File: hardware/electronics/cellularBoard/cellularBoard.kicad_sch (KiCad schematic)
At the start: 15 parts, among them J1 Standoff, J2 M.2_E_Key_PCB_Edge, U1 LM51571-Q1

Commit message: started on schematics
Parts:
- added C1: 2.2uF, symbol lib_sch:C
- added C11: 10nF, symbol lib_sch:C_horizontal
- added C12: 300pF, symbol lib_sch:C
- added C13: 1uF, symbol lib_sch:C_horizontal
- added C14: 10nF, symbol lib_sch:C
- added C15: 22uF, symbol lib_sch:C
- added C16, C2: 100nF, symbol lib_sch:C
- added D1: VAL, symbol DS-Diodes:D_Schottky_horizontal
- added L2: 680nH, symbol DS-Passives:L_horizontal
- added R1: 301R, symbol lib_sch:R
- added R2: 9K31, symbol lib_sch:R_horizontal
- added R3: 6K98, symbol lib_sch:R
- added R6: 2K49, symbol lib_sch:R
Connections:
- net VSS: now also U1.1 (PGND), U1.11 (MODE), U1.16 (PGND), U1.17 (AGND), U1.7 (AGND), C1.2, C11.1, C12.2, C13.1, C15.2, C16.2, C2.2, R1.2, R2.1
- net at U1.10 (SS): now also C11.2
- net at U1.12 (SW), U1.13 (SW), U1.14 (SW): now also D1.1, L2.2
- net at U1.2 (VCC): now also C13.2
- net at U1.3 (BIAS): now also U1.6 (UVLO), C1.1, C2.1, L2.1
- net at U1.5 (RT): now also R2.2
- net at U1.8 (COMP): now also C12.1, C14.1
- net at U1.9 (FB): now also R3.2, R6.1
- new net: C14.2, R1.1
- new net: C15.1, C16.1, D1.2, R3.1
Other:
- moved on the sheet: TP1, TP2, TP3, TP4, TP5, TP6, TP7, TP8, U1

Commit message: finished schematic
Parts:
- removed C11: 10nF, symbol lib_sch:C_horizontal
- removed C12: 300pF, symbol lib_sch:C
- removed C14: 10nF, symbol lib_sch:C
- removed C16: 100nF, symbol lib_sch:C
- removed R2: 9K31, symbol lib_sch:R_horizontal
- added C10, C19: 150pF, lib_fp:MLCC0603, symbol lib_sch:C
- added C11, C6, C9: 10nF, lib_fp:MLCC0603, symbol lib_sch:C
- added C5: 100nF, lib_fp:MLCC0603, symbol lib_sch:C
- added C7: 68pF, lib_fp:MLCC0603, symbol lib_sch:C
- added C8: 15pF, lib_fp:MLCC0603, symbol lib_sch:C
- added R3: 9K31, lib_fp:CRCW0402, symbol lib_sch:R
- added R5, R6: 10K, symbol lib_sch:R
- C1: footprint (none) -> lib_fp:MLCC0603; DKPN (none) -> 478-KAM15AR70J225KTCT-ND; MPN (none) -> KAM15AR70J225KT; Manufacturer (none) -> KYOCERA AVX; Package PKG -> 0603; Tolerance TOL -> 10%; Voltage Rating VOLTAGE -> 6V3
- C2: footprint (none) -> lib_fp:MLCC0603; DKPN (none) -> 478-KAM15AR71A104KTCT-ND; MPN (none) -> KAM15AR71A104KT; Manufacturer (none) -> KYOCERA AVX; Package PKG -> 0603; Tolerance TOL -> 10%; Voltage Rating VOLTAGE -> 10V
- C3: renamed from C13; footprint (none) -> lib_fp:MLCC0603; DKPN (none) -> 478-KAM15AR71A105KTCT-ND; MPN (none) -> KAM15AR71A105KT; Manufacturer (none) -> KYOCERA AVX; Package PKG -> 0603; Tolerace TOL -> 10%; Voltage Rating VOLT -> 10V
- C4: renamed from C15; DKPN (none) -> 478-KAM21AT70J226KUCT-ND; MPN (none) -> KAM21AT70J226KU; Manufacturer (none) -> KYOCERA AVX; Package PKG -> 0805; Tolerance TOL -> 10%; Voltage Rating VOLTAGE -> 6V3
- R1: renamed from R3; footprint (none) -> lib_fp:CRCW0402; DKPN (none) -> 541-6.98KLCT-ND; MPN (none) -> CRCW04026K98FKED; Manufacturer (none) -> Vishay Dale; Package PKG -> 0402; Power Rating PWR -> 62.5mW; Tolerance TOL -> 1%
- R2: renamed from R6; footprint (none) -> lib_fp:CRCW0402; DKPN (none) -> 541-2.49KLCT-ND; MPN (none) -> CRCW04022K49FKED; Manufacturer (none) -> Vishay Dale; Package PKG -> 0402; Power Rating PWR -> 62.5mW; Tolerance TOL -> 1%
- R4: renamed from R1; footprint (none) -> lib_fp:CRCW0402; DKPN (none) -> 541-301LCT-ND; MPN (none) -> CRCW0402301RFKED; Manufacturer (none) -> Vishay Dale; Package PKG -> 0402; Power Rating PWR -> 62.5mW; Tolerance TOL -> 1%
- renumbered L2 to L1, R4 to R7, R5 to R8
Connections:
- net +1V8: now also R5.1, R6.1
- net +3V3: now also C1.1, C2.1, L1.1, U1.3 (BIAS), U1.6 (UVLO)
- net SCL_1V8: now also R6.2
- net SDA_1V8: now also R5.2
- net VSS: now also R2.2, C10.2, C19.2, C5.2, C6.2, C7.2, C8.2, C9.2, R3.2
- net at R4.1: now also C11.2
- net at U1.8 (COMP): now also C10.1, C11.1, C19.1
- net +3V8: now reaches C4.1, D1.2, R1.1
- net +3V8: now also C5.1, C6.1, C7.1, C8.1
- net at U1.10 (SS): now also C9.1
- net at U1.5 (RT): now also R3.1
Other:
- moved on the sheet: C1, C2, C3, C4, D1, L1, R1, R2, R4, U1

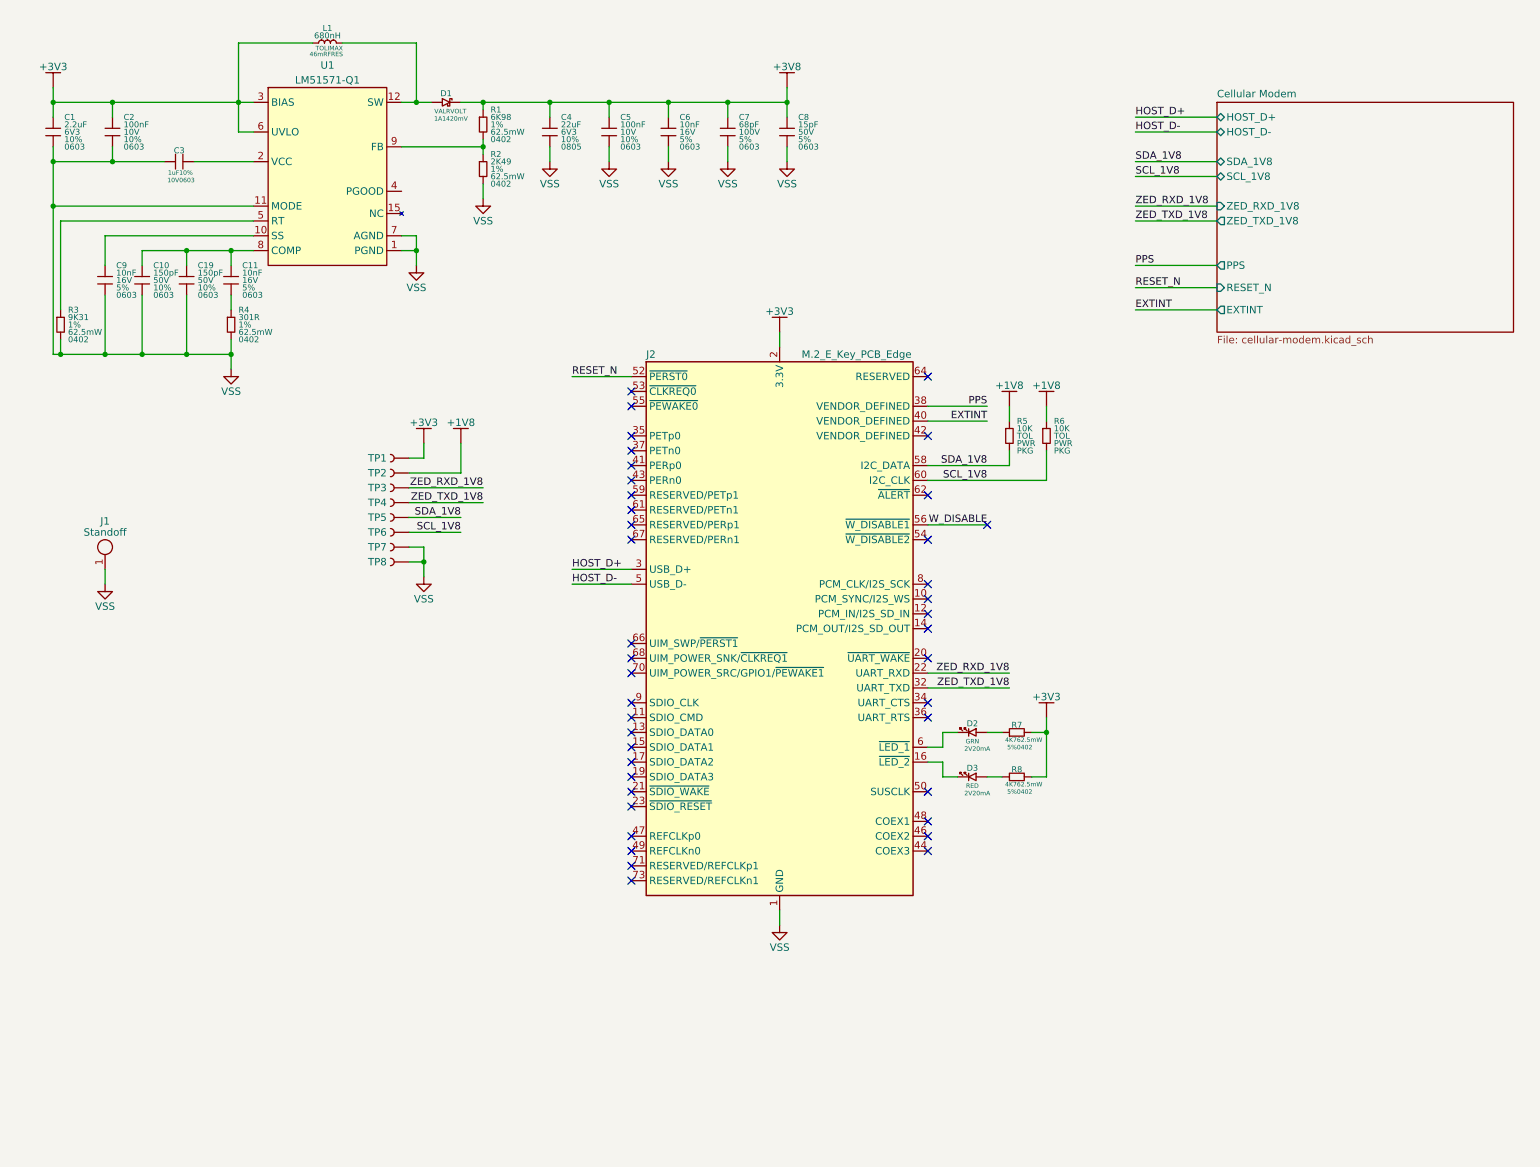
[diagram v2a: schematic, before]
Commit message: assigned footprints and worked on sch
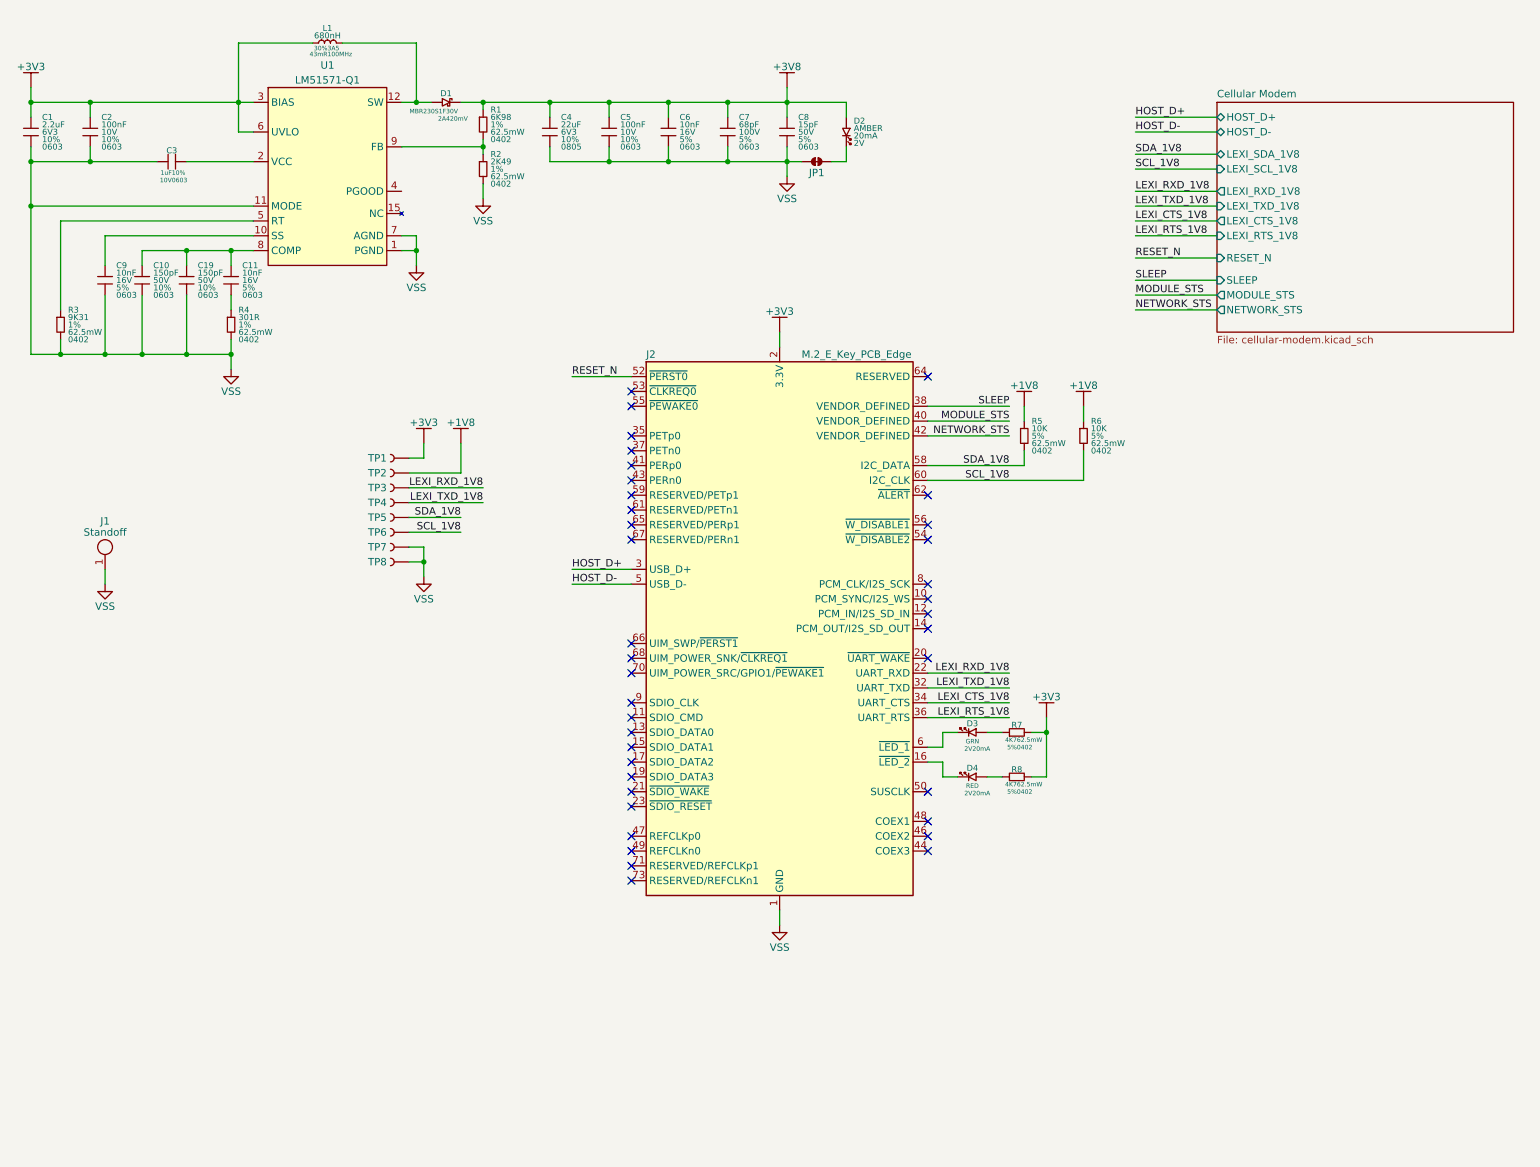
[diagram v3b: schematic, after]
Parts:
- added D2: LTST-C190KYKT, lib_fp:LTST-0603, symbol lib_sch:LED
- added JP1: ~, lib_fp:Jumper_2_Bridged, symbol lib_sch:Jumper_2_Bridged
- C4: footprint (none) -> lib_fp:MLCC0805
- D1: value VAL -> MBR230S1F; Current 1A1 -> 2A; DKPN (none) -> MBR230S1F-7DICT-ND; MPN (none) -> MBR230S1F-7; Manufacturer (none) -> Diodes Incorporated; Reverse Voltage RVOLT -> 30V
- L1: footprint (none) -> lib_fp:L_1212; Current Rating IMAX -> 3A5; DC Resistance 46mR -> 43mR; DKPN (none) -> 732-4953-1-ND; MPN (none) -> 744383340068; Manufacturer (none) -> Würth Elektronik; Resonant Frequency FRES -> 100MHz; Tolerance TOL -> 30%
- R5, R6: footprint (none) -> lib_fp:CRCW0402; DKPN (none) -> 541-10KJCT-ND; MPN (none) -> CRCW040210K0JNED; Manufacturer (none) -> Vishay Dale; Package PKG -> 0402; Power Rating PWR -> 62.5mW; Tolerance TOL -> 5%
- U1: footprint (none) -> lib_fp:RTE0016K; DKPN (none) -> 296-LM51571QRTERQ1CT-ND; MPN (none) -> LM51571QRTERQ1
- renumbered D2 to D3, D3 to D4
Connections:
- net +3V8: now also D2.1
- net VSS: now also JP1.1
- net LEXI_CTS_1V8: now reaches J2.34 (UART_CTS)
- net LEXI_RTS_1V8: now reaches J2.36 (UART_RTS)
- net NETWORK_STS: now reaches J2.42 (VENDOR_DEFINED)
- net EXTINT renamed MODULE_STS
- net PPS renamed SLEEP
- net W_DISABLE: no longer names the net of J2.56 (~{W_DISABLE1})
- net ZED_RXD_1V8 renamed LEXI_RXD_1V8
- net ZED_TXD_1V8 renamed LEXI_TXD_1V8
- new net: D2.2, JP1.2
- no-connect marks 41 -> 38
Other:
- sheet Cellular Modem ports: added LEXI_CTS_1V8, LEXI_RTS_1V8, LEXI_RXD_1V8, LEXI_SCL_1V8, LEXI_SDA_1V8, LEXI_TXD_1V8, MODULE_STS, NETWORK_STS, SLEEP; removed EXTINT, PPS, SCL_1V8, SDA_1V8, ZED_RXD_1V8, ZED_TXD_1V8
- moved on the sheet: C1, C2, C3, R5

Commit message: worked on LTE card
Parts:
- removed C10: 150pF, lib_fp:MLCC0603, symbol lib_sch:C
- C5: renamed from C19; value 150pF -> 330pF; DKPN 478-13033-1-ND -> 478-06035C331K4T2ACT-ND; MPN 06035C151K4T2A -> 06035C331K4T2A
- D1: footprint (none) -> lib_fp:SOD123F; symbol DS-Diodes:D_Schottky_horizontal -> lib_sch:D_Schottky_horizontal
- L1: footprint lib_fp:L_1212 -> lib_fp:L_0806; symbol DS-Passives:L_horizontal -> lib_sch:L_horizontal; Current Rating 3A5 -> 2A; DC Resistance 43mR -> 84mR; DKPN 732-4953-1-ND -> 732-5704-1-ND; MPN 744383340068 -> 744383430068; Resonant Frequency 100MHz -> 130MHz
- renumbered C7 to C10, C8 to C11, C9 to C4, C11 to C6, C4 to C7, C5 to C8, C6 to C9, R3 to R1, R4 to R2, R1 to R3, R2 to R4, R7 to R5, R8 to R6, R5 to R7, R6 to R8
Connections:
- net MODULE_STS: now also J2.42 (VENDOR_DEFINED); no longer J2.40 (VENDOR_DEFINED)
- net NETWORK_STS: now also J2.40 (VENDOR_DEFINED); no longer J2.42 (VENDOR_DEFINED)
- net SW: now reaches D1.1, L1.2, U1.12 (SW), U1.13 (SW), U1.14 (SW)
- net LEXI_CTS_1V8 renamed SARA_CTS_1V8
- net LEXI_RTS_1V8 renamed SARA_RTS_1V8
- net LEXI_RXD_1V8 renamed SARA_RXD_1V8
- net LEXI_TXD_1V8 renamed SARA_TXD_1V8
- net SCL_1V8 renamed SARA_SCL_1V8
- net SDA_1V8 renamed SARA_SDA_1V8
- no-connect marks 38 -> 39
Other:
- sheet Cellular Modem ports: added PPS, SARA_CTS_1V8, SARA_RTS_1V8, SARA_RXD_1V8, SARA_SCL_1V8, SARA_SDA_1V8, SARA_TXD_1V8; removed LEXI_CTS_1V8, LEXI_RTS_1V8, LEXI_RXD_1V8, LEXI_SCL_1V8, LEXI_SDA_1V8, LEXI_TXD_1V8
- moved on the sheet: C1, C2, C3, C4, R1
